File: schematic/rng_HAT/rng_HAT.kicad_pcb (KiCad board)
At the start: 2 copper layers, 25 parts, among them Q1 2N3904, Q2 2N3904, Q3 2N3904, Q4 BC107, Q5 2N3904, U1 RASPBERRY_PI_4B_4GB, U2 MAN72A, U3 STM32F103C8Tx

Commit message: working PCB?
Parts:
- removed U1: RASPBERRY_PI_4B_4GB, Module:Raspberry_Pi_Zero_Socketed_THT_FaceDown_MountingHoles
- removed U2: MAN72A, Display_7Segment:MAN72A
- added J1: RPi_GPIO, RPI_Hat:RPI_Hat_B+, F.Cu at (143.8, 93.0)
- D1, D2, D3: footprint LED_SMD:LED-APA102-2020 -> LED_SMD:LED_0201_0603Metric
- R1, R10, R2, R3, R4, R5, R6, R7, R8, R9: footprint OptoDevice:R_LDR_4.9x4.2mm_P2.54mm_Vertical -> Resistor_SMD:R_0201_0603Metric
- moved Q4 50.2 mm to (179.5, 70.5)
- moved D3 40.3 mm to (185.7, 79.6)
- moved C3 34.2 mm to (174.0, 69.1)
- moved D2 33.4 mm to (163.7, 80.0)
- moved C4 33.1 mm to (174.0, 75.1)
- moved C1 31.1 mm to (151.4, 66.8)
- moved D1 28.1 mm to (182.3, 119.5)
- moved C2 26.8 mm to (157.4, 73.3)
- moved R9 26.7 mm to (181.7, 64.6)
- moved Q5 21.2 mm to (185.5, 70.6)
- moved R10 19.8 mm to (179.5, 79.6)
- moved R8 19.6 mm to (177.2, 64.6)
- moved R7 16.3 mm to (175.0, 79.6)
- moved R5 15.6 mm to (167.2, 78.0)
- moved R6 11.7 mm to (173.2, 64.6)
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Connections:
- U3 pad 27: STREAM B -> STRM SPI(MOSI)
- U3 pad 28: Net-(U1-GPIO9/SPI_MISO) -> STRM SPI(MISO)
- U3 pad 45: I2C_clk -> STRM I2C(CLK)
- U3 pad 46: I2C_dt -> STRM I2C(DT)
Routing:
- net 5V: track 0.00 -> 117.9 mm
- net AN LED: track 0.00 -> 69.5 mm, vias 0 -> 1
- net WN LED: track 0.00 -> 64.1 mm
- net WN OUT: track 0.00 -> 52.0 mm
- net AN OUT: track 0.00 -> 46.6 mm, vias 0 -> 2
- net CS: track 0.00 -> 45.9 mm, vias 0 -> 1
- net Net-(D1-A): track 0.00 -> 39.4 mm
- net Net-(J1-BCM11_SCLK): track 0.00 -> 31.1 mm
- net Net-(Q5-C): track 0.00 -> 27.5 mm
- net STRM SPI(MOSI): track 0.00 -> 27.4 mm
- net STRM SPI(MISO): track 0.00 -> 25.8 mm, vias 0 -> 1
- net GND: track 0.00 -> 22.9 mm, vias 0 -> 8
- net STREAM A: track 0.00 -> 18.2 mm, vias 0 -> 1
- net Net-(Q1-E): track 0.00 -> 18.2 mm
- net INTRPT?: track 0.00 -> 18.1 mm, vias 0 -> 1
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- added copper zone on B.Cu, net GND
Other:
- board outline added: 56.5 x 65 mm

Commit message: different layer for serial lines and analog lines?
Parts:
- added C5: 2.2uF, Capacitor_SMD:CP_Elec_3x5.3, F.Cu at (149.5, 119.0)
- added J2: Conn_01x04_MountingPin, Connector_PinHeader_1.00mm:PinHeader_1x04_P1.00mm_Horizontal, F.Cu at (150.5, 123.0)
- added RN1: 930, Resistor_THT:R_Array_SIP6, F.Cu at (178.8, 85.0)
- added RN2: 930, Resistor_THT:R_Array_SIP6, F.Cu at (178.8, 99.5)
- added RN3: 930, Resistor_THT:R_Array_SIP6, F.Cu at (178.8, 89.5)
- added RN4: 930, Resistor_THT:R_Array_SIP6, F.Cu at (178.8, 95.0)
- moved D1 27.6 mm to (154.8, 117.0)
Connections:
- R10 pad 1: WN LED -> 5V
- R7 pad 1: WN LED -> 5V
- U3 pad 17: WN LED -> 5V
- U3 pad 34: unconnected-(U3-PA13-Pad34) -> SWDIO
- U3 pad 36: unconnected-(U3-VDD-Pad36) -> 3v3
- U3 pad 37: unconnected-(U3-PA14-Pad37) -> SWDCLK
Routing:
- net GND: track 22.9 -> 186.7 mm, vias 8 -> 7
- net 5V: track 117.9 -> 200.1 mm
- net WN LED: track 64.1 -> 0.00 mm
- net Net-(RN1-R5): track 0.00 -> 31.5 mm
- net SWDCLK: track 0.00 -> 28.8 mm, vias 0 -> 1
- net Net-(D1-A): track 39.4 -> 11.7 mm
- net SWDIO: track 0.00 -> 23.4 mm, vias 0 -> 1
- net 3v3: track 0.00 -> 3.30 mm, vias 0 -> 2
- added copper zone on B.Cu, net 3v3
- removed copper zone on B.Cu, net GND
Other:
- board text added: "Hw TRNG v1"
- board text added: "created by Akiel Aries"

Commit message: very broken! reverting and redoing
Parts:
- removed C5: 2.2uF, Capacitor_SMD:CP_Elec_3x5.3
- added C6: 2.2uF, Capacitor_SMD:CP_Elec_3x5.3, F.Cu at (172.0, 112.0)
- added D4: GREEN (ON), LED_SMD:LED_0201_0603Metric, F.Cu at (167.2, 118.0)
- added D5: CLEAR(TX), LED_SMD:LED_0201_0603Metric, F.Cu at (193.2, 101.8)
- added R11: 110, Resistor_SMD:R_0201_0603Metric, F.Cu at (189.2, 102.0)
- D1: value BLU (ON) -> BLU (FW ON)
- moved D1 16.8 mm to (171.7, 118.0)
- moved RN2 9.41 mm to (178.3, 90.1)
- moved RN3 4.97 mm to (178.3, 94.5)
- moved RN4 3.83 mm to (178.3, 98.8)
- moved J2 2.00 mm to (152.5, 123.1)
- moved RN1 0.89 mm to (178.3, 85.8)
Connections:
- R10 pad 1: 5V -> WN LED
- R7 pad 1: 5V -> WN LED
- RN1 pad 1: unconnected-(RN1-common-Pad1) -> JN OUT
- RN1 pad 6: Net-(RN1-R5) -> JN OUT
- RN2 pad 3: Net-(RN1-R5) -> JN OUT
- RN3 pad 2: Net-(RN1-R5) -> JN OUT
- RN4 pad 6: Net-(RN1-R5) -> JN OUT
- U3 pad 10: AN OUT -> RNG MUX
- U3 pad 14: AN LED -> AN OUT
- U3 pad 15: RNG MUX -> AN LED
- U3 pad 17: 5V -> WN LED
- U3 pad 29: unconnected-(U3-PA8-Pad29) -> JN OUT
- U3 pad 30: unconnected-(U3-PA9-Pad30) -> JN LED
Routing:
- net GND: track 186.7 -> 256.8 mm, vias 7 -> 13
- net JN OUT: track 0.00 -> 34.5 mm
- net Net-(RN1-R5): track 31.5 -> 0.00 mm
- net Net-(D1-A): track 11.7 -> 36.5 mm
- net 5V: track 200.1 -> 206.9 mm
- net Net-(D5-A): track 0.00 -> 4.42 mm
- net SWDCLK: track 28.8 -> 32.9 mm, vias 1 -> 2
- net 3v3: track 3.30 -> 5.34 mm, vias 2 -> 3
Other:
- board text added: "HRNG v1 STM32F103x based breakout"
- board text added: "by Akiel Aries 10/2024"
- board text removed: "Hw TRNG v1"
- board text removed: "created by Akiel Aries"

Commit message: working again. small changes
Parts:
- removed C6: 2.2uF, Capacitor_SMD:CP_Elec_3x5.3
- removed D5: CLEAR(TX), LED_SMD:LED_0201_0603Metric
- removed J2: Conn_01x04_MountingPin, Connector_PinHeader_1.00mm:PinHeader_1x04_P1.00mm_Horizontal
- removed R11: 110, Resistor_SMD:R_0201_0603Metric
- removed RN1, RN2, RN3, RN4: 930, Resistor_THT:R_Array_SIP6
- D4: value GREEN (ON) -> GRN (FW ON)
- moved D4 15.7 mm to (182.2, 122.5)
- moved D1 10.8 mm to (182.3, 119.5)
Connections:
- net 3v3 renamed 3V
- U3 pad 10: RNG MUX -> AN OUT
- U3 pad 14: AN OUT -> AN LED
- U3 pad 15: AN LED -> RNG MUX
- U3 pad 29: JN OUT -> unconnected-(U3-PA8-Pad29)
- U3 pad 30: JN LED -> unconnected-(U3-PA9-Pad30)
- U3 pad 34: SWDIO -> unconnected-(U3-PA13-Pad34)
- U3 pad 37: SWDCLK -> unconnected-(U3-PA14-Pad37)
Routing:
- net GND: track 256.8 -> 23.3 mm, vias 13 -> 9
- net 5V: track 206.9 -> 117.3 mm
- net WN LED: track 0.00 -> 63.9 mm
- net JN OUT: track 34.5 -> 0.00 mm
- net SWDCLK: track 32.9 -> 0.00 mm, vias 2 -> 0
- net 3V: track 5.34 -> 35.0 mm, vias 3 -> 2
- net SWDIO: track 23.4 -> 0.00 mm, vias 1 -> 0
- net Net-(D5-A): track 4.42 -> 0.00 mm
- net Net-(D1-A): track 36.5 -> 39.4 mm
- added copper zone on B.Cu, net GND
- removed copper zone on B.Cu, net 3V
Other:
- board text removed: "HRNG v1 STM32F103x based breakout"
- board text removed: "by Akiel Aries 10/2024"

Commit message: adding and running tests
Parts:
- added C5: 470uF, Capacitor_SMD:CP_Elec_3x5.3, F.Cu at (149.5, 118.0)
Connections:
- U3 pad 29: unconnected-(U3-PA8-Pad29) -> Net-(RN1-R2)
- U3 pad 30: unconnected-(U3-PA9-Pad30) -> Net-(U3-PA9)
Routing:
- net 5V: track 117.3 -> 121.6 mm
- net GND: track 23.3 -> 25.0 mm, vias 9 -> 10

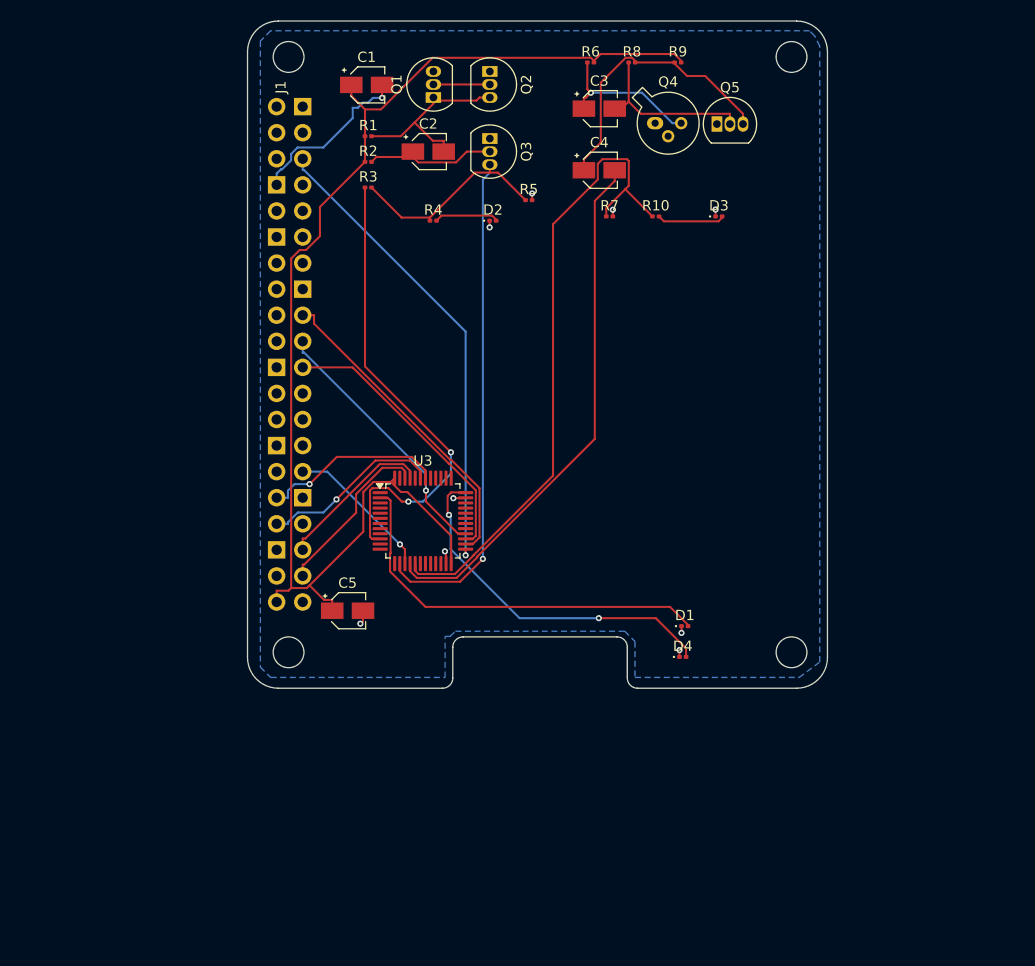
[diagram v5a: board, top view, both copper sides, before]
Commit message: reverting and starting over PCB. no routes
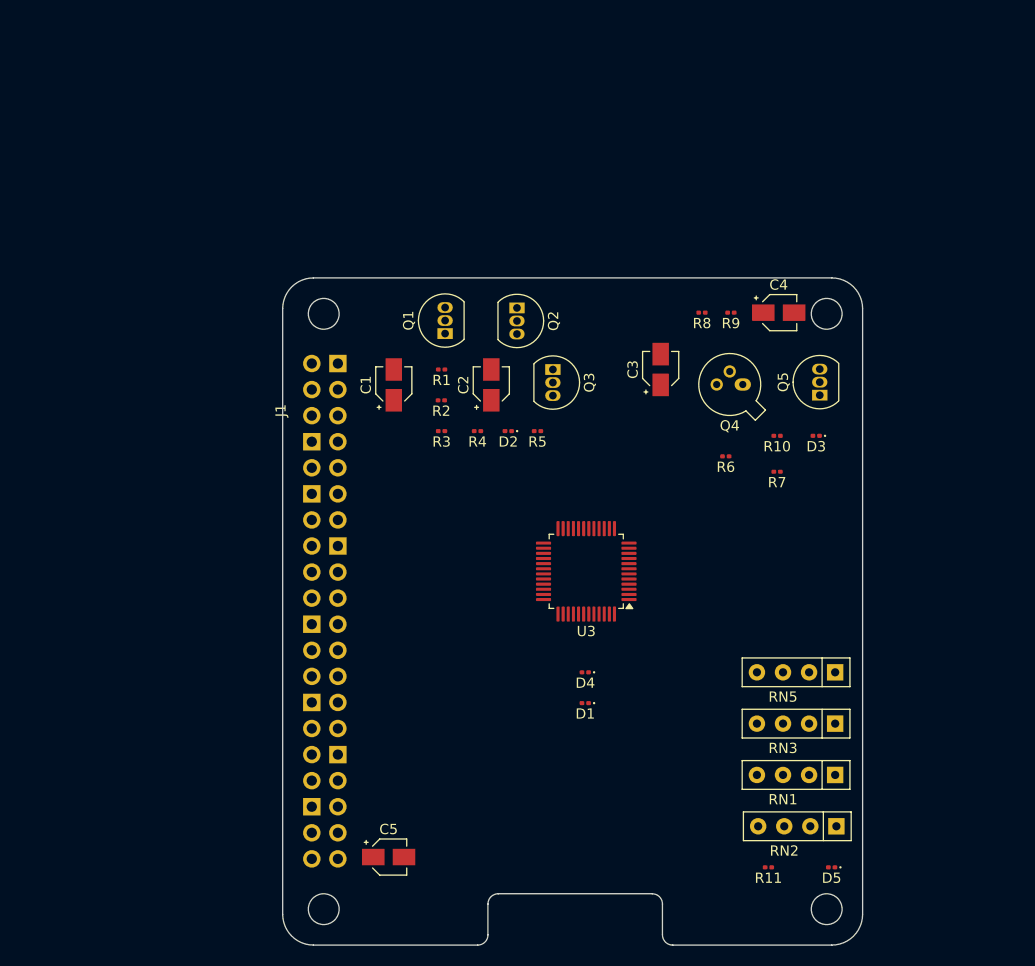
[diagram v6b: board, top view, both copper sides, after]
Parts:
- added D5: CLEAR(TX), LED_SMD:LED_0201_0603Metric, F.Cu at (196.7, 143.0)
- added R11: 110, Resistor_SMD:R_0201_0603Metric, F.Cu at (190.5, 143.0)
- added RN1: R_Network03, Resistor_THT:R_Array_SIP4, F.Cu at (197.0, 134.0)
- added RN2: R_Network03, Resistor_THT:R_Array_SIP4, F.Cu at (197.1, 139.0)
- added RN3: R_Network03, Resistor_THT:R_Array_SIP4, F.Cu at (197.0, 129.0)
- added RN5: R_Network03, Resistor_THT:R_Array_SIP4, F.Cu at (197.0, 124.0)
- moved R6 40.6 mm to (186.3, 103.0), turned to 180 degrees
- moved R7 29.8 mm to (191.3, 104.5), turned to 180 degrees
- moved C1 29.3 mm to (154.0, 96.0), turned to 90 degrees
- moved Q5 28.2 mm to (195.5, 97.0), turned to 90 degrees
- moved Q4 26.9 mm to (188.0, 96.0), turned to 180 degrees
- moved C3 26.1 mm to (180.0, 94.5), turned to 90 degrees
- moved R8 25.3 mm to (184.0, 89.0), turned to 180 degrees
- moved J1 25.3 mm to (147.2, 118.1)
- moved R9 24.9 mm to (186.8, 89.0), turned to 180 degrees
- moved R3 24.8 mm to (158.7, 100.5), turned to 180 degrees
- moved R10 24.4 mm to (191.3, 101.0), turned to 180 degrees
- moved C5 24.3 mm to (153.5, 142.0)
- moved R2 24.3 mm to (158.6, 97.5), turned to 180 degrees
- moved R1 23.8 mm to (158.7, 94.5), turned to 180 degrees
- moved C2 23.5 mm to (163.5, 96.0), turned to 90 degrees
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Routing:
- net 5V: track 121.6 -> 0.00 mm
- net AN LED: track 69.5 -> 0.00 mm, vias 1 -> 0
- net WN LED: track 64.1 -> 0.00 mm
- net WN OUT: track 52.0 -> 0.00 mm
- net AN OUT: track 46.6 -> 0.00 mm, vias 2 -> 0
- net CS: track 45.9 -> 0.00 mm, vias 1 -> 0
- net Net-(D1-A): track 39.4 -> 0.00 mm
- net 3V: track 35.0 -> 0.00 mm, vias 2 -> 0
- net Net-(J1-BCM11_SCLK): track 31.1 -> 0.00 mm
- net Net-(Q5-C): track 27.5 -> 0.00 mm
- net STRM SPI(MOSI): track 27.4 -> 0.00 mm
- net STRM SPI(MISO): track 25.8 -> 0.00 mm, vias 1 -> 0
- net GND: track 25.0 -> 0.00 mm, vias 10 -> 0
- net STREAM A: track 18.2 -> 0.00 mm, vias 1 -> 0
- net Net-(Q1-E): track 18.2 -> 0.00 mm
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- removed copper zone on B.Cu, net GND

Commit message: some more PCB updates
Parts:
- added C6: 10uF, Capacitor_SMD:C_0603_1608Metric_Pad1.08x0.95mm_HandSolder, F.Cu at (168.0, 86.1)
- added C7: 104nF, Capacitor_SMD:C_0603_1608Metric_Pad1.08x0.95mm_HandSolder, F.Cu at (168.4, 145.0)
- added C8: 20pF, Capacitor_SMD:C_0603_1608Metric_Pad1.08x0.95mm_HandSolder, F.Cu at (183.2, 124.5)
- added J2: Conn_01x04_Pin, Connector_PinHeader_1.00mm:PinHeader_1x04_P1.00mm_Horizontal, F.Cu at (176.0, 145.6)
- added R12: 1M, Resistor_SMD:R_0201_0603Metric, F.Cu at (186.0, 123.0)
- added Y2: 8MHz, Crystal:Crystal_SMD_3215-2Pin_3.2x1.5mm, F.Cu at (188.5, 123.2)
- C1: value 10uF -> 0.1uF; footprint Capacitor_SMD:CP_Elec_3x5.3 -> Capacitor_SMD:C_0603_1608Metric_Pad1.08x0.95mm_HandSolder
- C2: value 0.1uF -> 2.2uF; footprint Capacitor_SMD:CP_Elec_3x5.3 -> Capacitor_SMD:C_0603_1608Metric_Pad1.08x0.95mm_HandSolder
- C3: value 100nF -> 20pF; footprint Capacitor_SMD:CP_Elec_3x5.3 -> Capacitor_SMD:C_0603_1608Metric_Pad1.08x0.95mm_HandSolder
- C4: value 2.2uF -> 100nF; footprint Capacitor_SMD:CP_Elec_3x5.3 -> Capacitor_SMD:C_0603_1608Metric_Pad1.08x0.95mm_HandSolder
- D4: value GRN (FW ON) -> GRN (PWR ON)
- moved C2 47.7 mm to (211.0, 92.0), turned to -90 degrees
- moved C3 27.7 mm to (183.2, 122.0), turned to 0 degrees
- moved R6 23.1 mm to (200.8, 85.0)
- moved R11 22.0 mm to (207.0, 128.5)
- moved R8 20.5 mm to (204.5, 88.5)
- moved RN2 20.2 mm to (211.6, 124.9)
- moved RN1 20.0 mm to (211.6, 120.4)
- moved D5 19.7 mm to (210.0, 128.5)
- moved RN3 19.7 mm to (211.6, 115.8)
- moved RN5 19.2 mm to (211.6, 111.5)
- moved C1 18.7 mm to (172.0, 91.0), turned to 180 degrees
- moved R9 18.1 mm to (204.5, 85.0)
- moved R10 17.1 mm to (207.8, 96.5)
- moved C5 15.3 mm to (168.5, 139.0)
- moved J1 15.1 mm to (161.9, 115.1)
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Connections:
- C1 pad 1: 5V -> Net-(Q1-E)
- C1 pad 2: GND -> Net-(Q3-B)
- C2 pad 1: Net-(Q3-B) -> Net-(Q5-C)
- C2 pad 2: Net-(Q1-E) -> WN OUT
- C3 pad 1: Net-(Q4-C) -> GND
- C3 pad 2: Net-(Q5-B) -> Net-(U3-PD1)
- C4 pad 1: Net-(Q5-C) -> Net-(Q4-C)
- C4 pad 2: WN OUT -> Net-(Q5-B)
- U3 pad 34: unconnected-(U3-PA13-Pad34) -> Net-(J2-Pin_2)
- U3 pad 37: unconnected-(U3-PA14-Pad37) -> Net-(J2-Pin_3)
- U3 pad 5: unconnected-(U3-PD0-Pad5) -> Net-(U3-PD0)
- U3 pad 6: unconnected-(U3-PD1-Pad6) -> Net-(U3-PD1)
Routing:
- added copper zone on B.Cu, net GND
